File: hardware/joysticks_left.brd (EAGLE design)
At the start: 64.8 x 87.6 mm, 11 parts, among them IC1 MEGA16-M

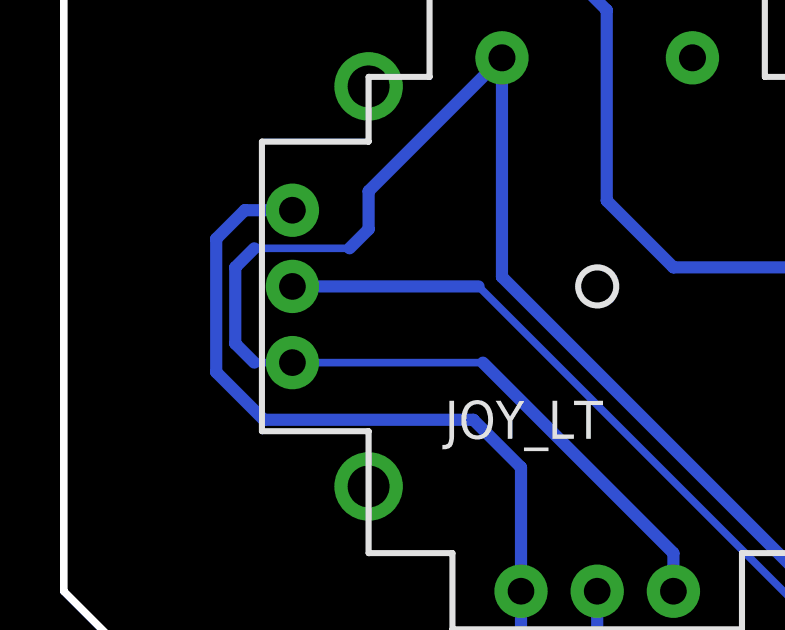
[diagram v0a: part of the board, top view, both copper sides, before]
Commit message: minor layout tuning due to etching fuckup
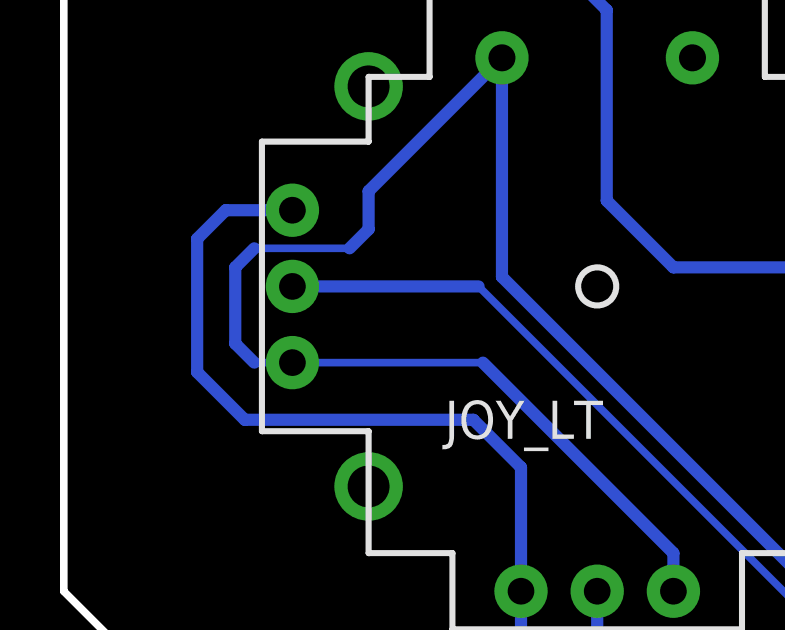
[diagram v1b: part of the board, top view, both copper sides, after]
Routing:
- net VCC: track 218.4 -> 219.6 mm
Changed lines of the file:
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@@
 <wire x1="23.495" y1="52.3875" x2="33.02" y2="52.3875" width="0.4064" layer="16"/>
 <wire x1="33.02" y1="52.3875" x2="34.29" y2="53.6575" width="0.4064" layer="16"/>
-<polygon width="0.254" layer="16" isolate="0.3048">
+<polygon width="0.254" layer="16" isolate="0.4064">
 <vertex x="-1.27" y="72.39"/>
 <vertex x="-1.27" y="52.07"/>
@@
 <wire x1="41.5925" y1="51.435" x2="40.1075" y2="49.95" width="0.254" layer="16"/>
 <wire x1="40.1075" y1="49.95" x2="39.0525" y2="49.95" width="0.254" layer="16"/>
-<wire x1="6.35" y1="64.77" x2="4.7625" y2="64.77" width="0.4064" layer="16"/>
-<wire x1="4.7625" y1="64.77" x2="3.81" y2="63.8175" width="0.4064" layer="16"/>
-<wire x1="3.81" y1="63.8175" x2="3.81" y2="59.3725" width="0.4064" layer="16"/>
-<wire x1="3.81" y1="59.3725" x2="5.3975" y2="57.785" width="0.4064" layer="16"/>
-<wire x1="5.3975" y1="57.785" x2="12.3825" y2="57.785" width="0.4064" layer="16"/>
+<wire x1="6.35" y1="64.77" x2="4.1275" y2="64.77" width="0.4064" layer="16"/>
+<wire x1="4.1275" y1="64.77" x2="3.175" y2="63.8175" width="0.4064" layer="16"/>
+<wire x1="3.175" y1="63.8175" x2="3.175" y2="59.3725" width="0.4064" layer="16"/>
+<wire x1="3.175" y1="59.3725" x2="4.7625" y2="57.785" width="0.4064" layer="16"/>
+<wire x1="4.7625" y1="57.785" x2="12.3825" y2="57.785" width="0.4064" layer="16"/>
 <wire x1="12.3825" y1="57.785" x2="13.97" y2="56.1975" width="0.4064" layer="16"/>
 <wire x1="13.97" y1="56.1975" x2="13.97" y2="52.07" width="0.4064" layer="16"/>

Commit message: set value for xtal-caps
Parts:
- C1, C2: value (none) -> 18p
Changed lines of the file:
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@@
 </element>
 <element name="U$1" library="jocki" package="ABM2" value="CRYSTALABM2" x="43.18" y="45.72" rot="MR90"/>
-<element name="C1" library="rcl" package="C0603" value="" x="48.26" y="48.26" rot="MR90"/>
-<element name="C2" library="rcl" package="C0603" value="" x="48.26" y="43.18" rot="MR270"/>
+<element name="C1" library="rcl" package="C0603" value="18p" x="48.26" y="48.26" rot="MR90"/>
+<element name="C2" library="rcl" package="C0603" value="18p" x="48.26" y="43.18" rot="MR270"/>
 <element name="SV1" library="con-lstb" package="MA05-2" value="" x="54.61" y="45.72" rot="R270">
 <attribute name="OC_NEWARK" value="unknown" x="21.59" y="-1.27" size="1.778" layer="27" rot="R270" display="off"/>
